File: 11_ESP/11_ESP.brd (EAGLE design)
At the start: 67.4 x 44.8 mm, 8 parts, among them T1 BC847, T2 BC847, X1 ALLSERIALSLAVE

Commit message: Use lib elements
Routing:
- removed copper zone on layer 16, net N$10
- removed copper zone on layer 16, net N$11
- removed copper zone on layer 1, net N$13
- removed copper zone on layer 16, net N$13
- removed copper zone on layer 1, net N$14
- removed copper zone on layer 16, net N$14
- removed copper zone on layer 1, net N$15
- removed copper zone on layer 16, net N$15
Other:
- board text added: "AllSerial ESP PROG v1.0 44/18"
- board text removed: "AllSerial ESP PROG v1.1 46/18"
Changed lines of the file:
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@@
 <?xml version="1.0" encoding="utf-8"?>
 <!DOCTYPE eagle SYSTEM "eagle.dtd">
-<eagle version="7.7.0">
+<eagle version="7.6.0">
 <drawing>
 <settings>
@@
 <grid distance="1.27" unitdist="mm" unit="mm" style="lines" multiple="1" display="yes" altdistance="0.025" altunitdist="inch" altunit="inch"/>
 <layers>
-<layer number="1" name="Top" color="4" fill="1" visible="yes" active="yes"/>
+<layer number="1" name="Top" color="4" fill="1" visible="no" active="yes"/>
 <layer number="2" name="Route2" color="1" fill="3" visible="no" active="no"/>
 <layer number="3" name="Route3" color="4" fill="3" visible="no" active="no"/>
@@
 <layer number="14" name="Route14" color="1" fill="6" visible="no" active="no"/>
 <layer number="15" name="Route15" color="4" fill="6" visible="no" active="no"/>
-<layer number="16" name="Bottom" color="1" fill="1" visible="yes" active="yes"/>
+<layer number="16" name="Bottom" color="1" fill="1" visible="no" active="yes"/>
 <layer number="17" name="Pads" color="2" fill="1" visible="yes" active="yes"/>
-<layer number="18" name="Vias" color="2" fill="1" visible="yes" active="yes"/>
+<layer number="18" name="Vias" color="2" fill="1" visible="no" active="yes"/>
 <layer number="19" name="Unrouted" color="6" fill="1" visible="yes" active="yes"/>
 <layer number="20" name="Dimension" color="15" fill="1" visible="yes" active="yes"/>
@@
 <layer number="24" name="bOrigins" color="15" fill="1" visible="no" active="yes"/>
 <layer number="25" name="tNames" color="7" fill="1" visible="yes" active="yes"/>
-<layer number="26" name="bNames" color="7" fill="1" visible="yes" active="yes"/>
+<layer number="26" name="bNames" color="7" fill="1" visible="no" active="yes"/>
 <layer number="27" name="tValues" color="7" fill="1" visible="yes" active="yes"/>
 <layer number="28" name="bValues" color="7" fill="1" visible="no" active="yes"/>
-<layer number="29" name="tStop" color="7" fill="3" visible="yes" active="yes"/>
-<layer number="30" name="bStop" color="7" fill="6" visible="yes" active="yes"/>
+<layer number="29" name="tStop" color="7" fill="3" visible="no" active="yes"/>
+<layer number="30" name="bStop" color="7" fill="6" visible="no" active="yes"/>
 <layer number="31" name="tCream" color="7" fill="4" visible="no" active="yes"/>
 <layer number="32" name="bCream" color="7" fill="5" visible="no" active="yes"/>
@@
 <board>
 <plain>
-<text x="-29.845" y="1.27" size="1.6764" layer="21" rot="R90">AllSerial ESP PROG v1.1 46/18</text>
-<polygon width="0.254" layer="29">
-<vertex x="-25.4" y="44.45"/>
-<vertex x="-28.575" y="44.45"/>
-<vertex x="-28.575" y="41.91"/>
-<vertex x="-25.4" y="41.91"/>
-</polygon>
-<polygon width="0.254" layer="29">
-<vertex x="-2.54" y="44.45"/>
-<vertex x="2.54" y="44.45"/>
-<vertex x="2.54" y="41.91"/>
-<vertex x="-2.54" y="41.91"/>
-</polygon>
-<polygon width="0.254" layer="29">
-<vertex x="25.4" y="44.45"/>
-<vertex x="28.575" y="44.45"/>
-<vertex x="28.575" y="41.91"/>
-<vertex x="25.4" y="41.91"/>
-</polygon>
-<polygon width="0.254" layer="30">
-<vertex x="-29.21" y="44.45"/>
-<vertex x="-25.4" y="44.45"/>
-<vertex x="-25.4" y="41.91"/>
-<vertex x="-29.21" y="41.91"/>
-</polygon>
-<polygon width="0.254" layer="30">
-<vertex x="-15.24" y="44.45"/>
-<vertex x="-11.43" y="44.45"/>
-<vertex x="-11.43" y="41.91"/>
-<vertex x="-15.24" y="41.91"/>
-</polygon>
-<polygon width="0.254" layer="30">
-<vertex x="-2.54" y="44.45"/>
-<vertex x="2.54" y="44.45"/>
-<vertex x="2.54" y="41.91"/>
-<vertex x="-2.54" y="41.91"/>
-</polygon>
-<polygon width="0.254" layer="30">
-<vertex x="11.43" y="44.45"/>
-<vertex x="15.24" y="44.45"/>
-<vertex x="15.24" y="41.91"/>
-<vertex x="11.43" y="41.91"/>
-</polygon>
-<polygon width="0.254" layer="30">
-<vertex x="25.4" y="44.45"/>
-<vertex x="29.21" y="44.45"/>
-<vertex x="29.21" y="41.91"/>
-<vertex x="25.4" y="41.91"/>
-</polygon>
+<text x="-29.845" y="1.27" size="1.6764" layer="21" rot="R90">AllSerial ESP PROG v1.0 44/18</text>
+<rectangle x1="-8.89" y1="43.815" x2="-3.81" y2="45.72" layer="29"/>
+<rectangle x1="-25.4" y1="43.815" x2="-20.32" y2="45.72" layer="29"/>
+<rectangle x1="-1.27" y1="43.815" x2="3.81" y2="45.72" layer="29"/>
+<rectangle x1="21.59" y1="43.815" x2="26.67" y2="45.72" layer="29"/>
+<rectangle x1="-2.54" y1="43.815" x2="2.54" y2="45.72" layer="30"/>
+<rectangle x1="-12.7" y1="43.815" x2="-7.62" y2="45.72" layer="30"/>
+<rectangle x1="-22.86" y1="43.815" x2="-17.78" y2="45.72" layer="30"/>
+<rectangle x1="7.62" y1="43.815" x2="12.7" y2="45.72" layer="30"/>
+<rectangle x1="17.78" y1="43.815" x2="22.86" y2="45.72" layer="30"/>
 </plain>
 <attributes>
@@
 <signal name="GND">
 <polygon width="0.254" layer="16">
-<vertex x="-34.29" y="40.64"/>
-<vertex x="34.29" y="40.64"/>
+<vertex x="-34.29" y="45.72"/>
+<vertex x="34.29" y="45.72"/>
 <vertex x="34.29" y="0"/>
 <vertex x="-34.29" y="0"/>
@@
 <vertex x="-34.29" y="0"/>
 <vertex x="34.29" y="0"/>
-<vertex x="34.29" y="40.64"/>
-<vertex x="-34.29" y="40.64"/>
+<vertex x="34.29" y="45.72"/>
+<vertex x="-34.29" y="45.72"/>
 </polygon>
 <contactref element="X1" pad="1"/>
-<via x="-7.62" y="39.37" extent="1-16" drill="0.3"/>
-<via x="-17.78" y="39.37" extent="1-16" drill="0.3"/>
-<via x="-27.94" y="39.37" extent="1-16" drill="0.3"/>
+<via x="-7.62" y="43.18" extent="1-16" drill="0.3"/>
+<via x="-17.78" y="43.18" extent="1-16" drill="0.3"/>
+<via x="-27.94" y="43.18" extent="1-16" drill="0.3"/>
 <via x="-27.94" y="35.56" extent="1-16" drill="0.3"/>
 <via x="-17.78" y="35.56" extent="1-16" drill="0.3"/>
@@
 <via x="7.62" y="30.48" extent="1-16" drill="0.3"/>
 <via x="7.62" y="35.56" extent="1-16" drill="0.3"/>
-<via x="7.62" y="39.37" extent="1-16" drill="0.3"/>
-<via x="17.78" y="39.37" extent="1-16" drill="0.3"/>
+<via x="7.62" y="43.18" extent="1-16" drill="0.3"/>
+<via x="17.78" y="43.18" extent="1-16" drill="0.3"/>
 <via x="17.78" y="35.56" extent="1-16" drill="0.3"/>
-<via x="27.94" y="39.37" extent="1-16" drill="0.3"/>
+<via x="27.94" y="43.18" extent="1-16" drill="0.3"/>
 <via x="27.94" y="35.56" extent="1-16" drill="0.3"/>
 <via x="17.78" y="25.4" extent="1-16" drill="0.3"/>
@@
 <wire x1="6.35" y1="2.54" x2="6.35" y2="4.445" width="0.3048" layer="1"/>
 </signal>
-<signal name="N$13">
-<polygon width="0.254" layer="16">
-<vertex x="-25.4" y="44.45"/>
-<vertex x="-29.21" y="44.45"/>
-<vertex x="-29.21" y="41.91"/>
-<vertex x="-25.4" y="41.91"/>
-</polygon>
-<polygon width="0.254" layer="1">
-<vertex x="-25.4" y="44.45"/>
-<vertex x="-28.575" y="44.45"/>
-<vertex x="-28.575" y="41.91"/>
-<vertex x="-25.4" y="41.91"/>
-</polygon>
-<via x="-26.035" y="43.18" extent="1-16" drill="0.3"/>
-<via x="-27.94" y="43.18" extent="1-16" drill="0.3"/>
-</signal>
-<signal name="N$14">
-<polygon width="0.254" layer="16">
-<vertex x="-2.54" y="44.45"/>
-<vertex x="2.54" y="44.45"/>
-<vertex x="2.54" y="41.91"/>
-<vertex x="-2.54" y="41.91"/>
-</polygon>
-<polygon width="0.254" layer="1">
-<vertex x="-2.54" y="44.45"/>
-<vertex x="2.54" y="44.45"/>
-<vertex x="2.54" y="41.91"/>
-<vertex x="-2.54" y="41.91"/>
-</polygon>
-<via x="0" y="43.18" extent="1-16" drill="0.3"/>
-<via x="-1.905" y="43.18" extent="1-16" drill="0.3"/>
-<via x="1.905" y="43.18" extent="1-16" drill="0.3"/>
-</signal>
-<signal name="N$15">
-<polygon width="0.254" layer="16">
-<vertex x="25.4" y="44.45"/>
-<vertex x="29.21" y="44.45"/>
-<vertex x="29.21" y="41.91"/>
-<vertex x="25.4" y="41.91"/>
-</polygon>
-<polygon width="0.254" layer="1">
-<vertex x="25.4" y="44.45"/>
-<vertex x="28.575" y="44.45"/>
-<vertex x="28.575" y="41.91"/>
-<vertex x="25.4" y="41.91"/>
-</polygon>
-<via x="26.035" y="43.18" extent="1-16" drill="0.3"/>
-<via x="27.94" y="43.18" extent="1-16" drill="0.3"/>
-</signal>
-<signal name="N$10">
-<polygon width="0.254" layer="16">
-<vertex x="-15.24" y="44.45"/>
-<vertex x="-11.43" y="44.45"/>
-<vertex x="-11.43" y="41.91"/>
-<vertex x="-15.24" y="41.91"/>
-</polygon>
-<via x="-13.335" y="43.18" extent="1-16" drill="0.3"/>
-<via x="-14.605" y="43.18" extent="1-16" drill="0.3"/>
-<via x="-12.065" y="43.18" extent="1-16" drill="0.3"/>
-</signal>
-<signal name="N$11">
-<polygon width="0.254" layer="16">
-<vertex x="11.43" y="44.45"/>
-<vertex x="15.24" y="44.45"/>
-<vertex x="15.24" y="41.91"/>
-<vertex x="11.43" y="41.91"/>
-</polygon>
-<via x="13.335" y="43.18" extent="1-16" drill="0.3"/>
-<via x="12.065" y="43.18" extent="1-16" drill="0.3"/>
-<via x="14.605" y="43.18" extent="1-16" drill="0.3"/>
-</signal>
 </signals>

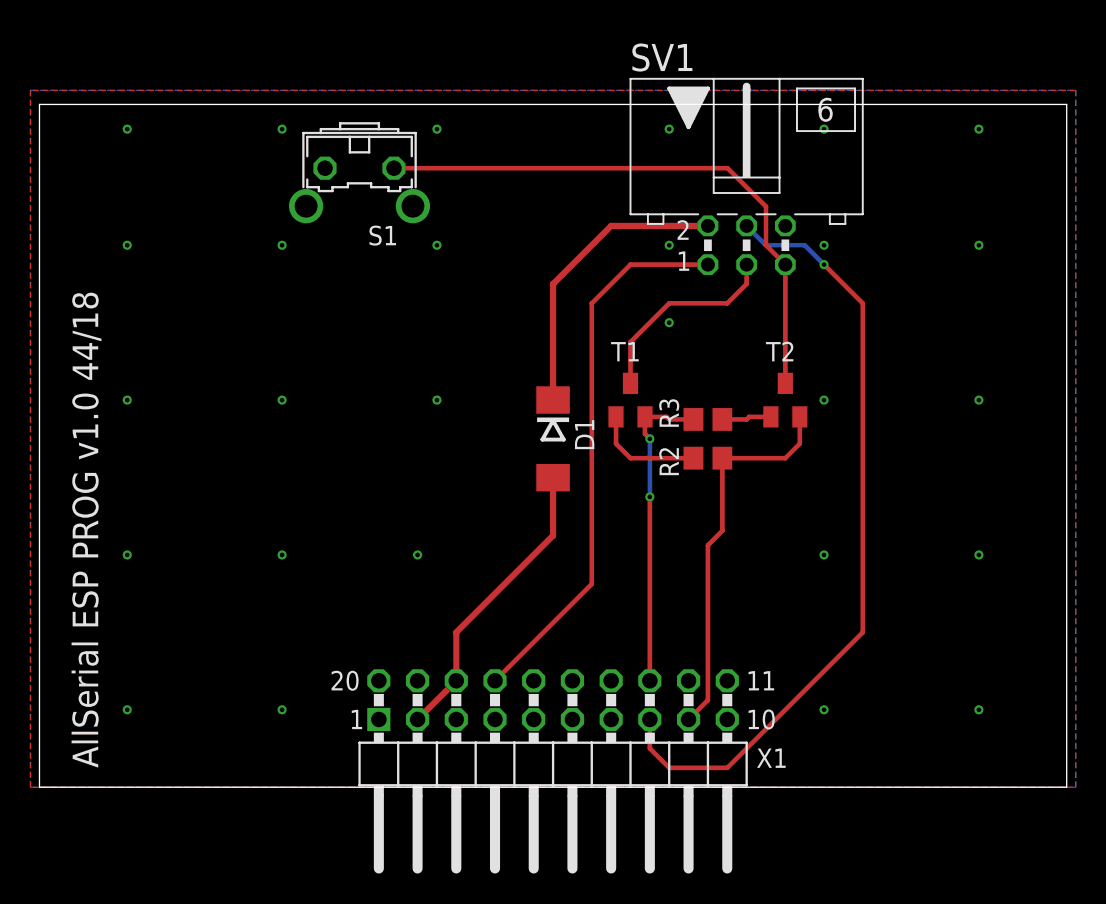
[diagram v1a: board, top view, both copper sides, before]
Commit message: pro mini layout corrected
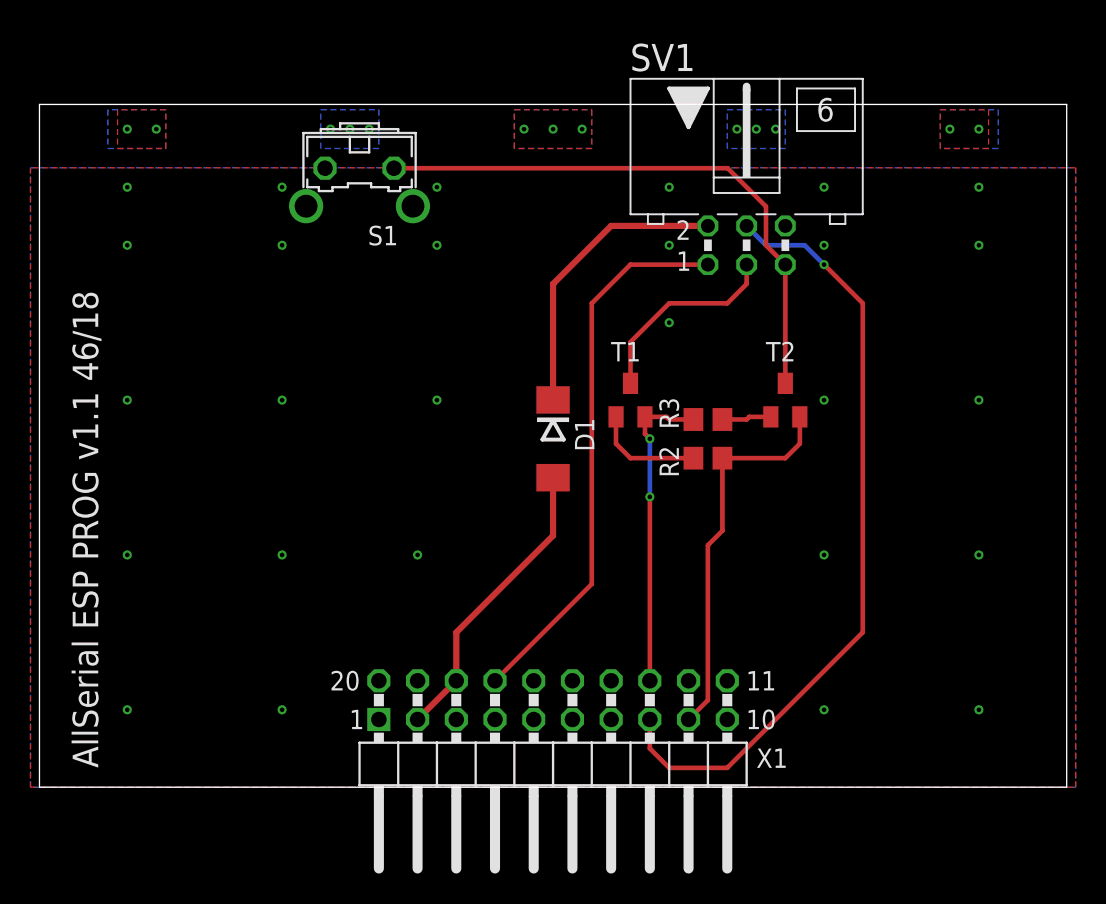
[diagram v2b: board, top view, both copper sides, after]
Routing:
- added copper zone on layer 16, net N$10
- added copper zone on layer 16, net N$11
- added copper zone on layer 1, net N$13
- added copper zone on layer 16, net N$13
- added copper zone on layer 1, net N$14
- added copper zone on layer 16, net N$14
- added copper zone on layer 1, net N$15
- added copper zone on layer 16, net N$15
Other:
- board text added: "AllSerial ESP PROG v1.1 46/18"
- board text removed: "AllSerial ESP PROG v1.0 44/18"
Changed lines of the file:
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@@
 <?xml version="1.0" encoding="utf-8"?>
 <!DOCTYPE eagle SYSTEM "eagle.dtd">
-<eagle version="7.6.0">
+<eagle version="7.7.0">
 <drawing>
 <settings>
@@
 <grid distance="1.27" unitdist="mm" unit="mm" style="lines" multiple="1" display="yes" altdistance="0.025" altunitdist="inch" altunit="inch"/>
 <layers>
-<layer number="1" name="Top" color="4" fill="1" visible="no" active="yes"/>
+<layer number="1" name="Top" color="4" fill="1" visible="yes" active="yes"/>
 <layer number="2" name="Route2" color="1" fill="3" visible="no" active="no"/>
 <layer number="3" name="Route3" color="4" fill="3" visible="no" active="no"/>
@@
 <layer number="14" name="Route14" color="1" fill="6" visible="no" active="no"/>
 <layer number="15" name="Route15" color="4" fill="6" visible="no" active="no"/>
-<layer number="16" name="Bottom" color="1" fill="1" visible="no" active="yes"/>
+<layer number="16" name="Bottom" color="1" fill="1" visible="yes" active="yes"/>
 <layer number="17" name="Pads" color="2" fill="1" visible="yes" active="yes"/>
-<layer number="18" name="Vias" color="2" fill="1" visible="no" active="yes"/>
+<layer number="18" name="Vias" color="2" fill="1" visible="yes" active="yes"/>
 <layer number="19" name="Unrouted" color="6" fill="1" visible="yes" active="yes"/>
 <layer number="20" name="Dimension" color="15" fill="1" visible="yes" active="yes"/>
@@
 <layer number="24" name="bOrigins" color="15" fill="1" visible="no" active="yes"/>
 <layer number="25" name="tNames" color="7" fill="1" visible="yes" active="yes"/>
-<layer number="26" name="bNames" color="7" fill="1" visible="no" active="yes"/>
+<layer number="26" name="bNames" color="7" fill="1" visible="yes" active="yes"/>
 <layer number="27" name="tValues" color="7" fill="1" visible="yes" active="yes"/>
 <layer number="28" name="bValues" color="7" fill="1" visible="no" active="yes"/>
-<layer number="29" name="tStop" color="7" fill="3" visible="no" active="yes"/>
-<layer number="30" name="bStop" color="7" fill="6" visible="no" active="yes"/>
+<layer number="29" name="tStop" color="7" fill="3" visible="yes" active="yes"/>
+<layer number="30" name="bStop" color="7" fill="6" visible="yes" active="yes"/>
 <layer number="31" name="tCream" color="7" fill="4" visible="no" active="yes"/>
 <layer number="32" name="bCream" color="7" fill="5" visible="no" active="yes"/>
@@
 <board>
 <plain>
-<text x="-29.845" y="1.27" size="1.6764" layer="21" rot="R90">AllSerial ESP PROG v1.0 44/18</text>
-<rectangle x1="-8.89" y1="43.815" x2="-3.81" y2="45.72" layer="29"/>
-<rectangle x1="-25.4" y1="43.815" x2="-20.32" y2="45.72" layer="29"/>
-<rectangle x1="-1.27" y1="43.815" x2="3.81" y2="45.72" layer="29"/>
-<rectangle x1="21.59" y1="43.815" x2="26.67" y2="45.72" layer="29"/>
-<rectangle x1="-2.54" y1="43.815" x2="2.54" y2="45.72" layer="30"/>
-<rectangle x1="-12.7" y1="43.815" x2="-7.62" y2="45.72" layer="30"/>
-<rectangle x1="-22.86" y1="43.815" x2="-17.78" y2="45.72" layer="30"/>
-<rectangle x1="7.62" y1="43.815" x2="12.7" y2="45.72" layer="30"/>
-<rectangle x1="17.78" y1="43.815" x2="22.86" y2="45.72" layer="30"/>
+<text x="-29.845" y="1.27" size="1.6764" layer="21" rot="R90">AllSerial ESP PROG v1.1 46/18</text>
+<polygon width="0.254" layer="29">
+<vertex x="-25.4" y="44.45"/>
+<vertex x="-28.575" y="44.45"/>
+<vertex x="-28.575" y="41.91"/>
+<vertex x="-25.4" y="41.91"/>
+</polygon>
+<polygon width="0.254" layer="29">
+<vertex x="-2.54" y="44.45"/>
+<vertex x="2.54" y="44.45"/>
+<vertex x="2.54" y="41.91"/>
+<vertex x="-2.54" y="41.91"/>
+</polygon>
+<polygon width="0.254" layer="29">
+<vertex x="25.4" y="44.45"/>
+<vertex x="28.575" y="44.45"/>
+<vertex x="28.575" y="41.91"/>
+<vertex x="25.4" y="41.91"/>
+</polygon>
+<polygon width="0.254" layer="30">
+<vertex x="-29.21" y="44.45"/>
+<vertex x="-25.4" y="44.45"/>
+<vertex x="-25.4" y="41.91"/>
+<vertex x="-29.21" y="41.91"/>
+</polygon>
+<polygon width="0.254" layer="30">
+<vertex x="-15.24" y="44.45"/>
+<vertex x="-11.43" y="44.45"/>
+<vertex x="-11.43" y="41.91"/>
+<vertex x="-15.24" y="41.91"/>
+</polygon>
+<polygon width="0.254" layer="30">
+<vertex x="-2.54" y="44.45"/>
+<vertex x="2.54" y="44.45"/>
+<vertex x="2.54" y="41.91"/>
+<vertex x="-2.54" y="41.91"/>
+</polygon>
+<polygon width="0.254" layer="30">
+<vertex x="11.43" y="44.45"/>
+<vertex x="15.24" y="44.45"/>
+<vertex x="15.24" y="41.91"/>
+<vertex x="11.43" y="41.91"/>
+</polygon>
+<polygon width="0.254" layer="30">
+<vertex x="25.4" y="44.45"/>
+<vertex x="29.21" y="44.45"/>
+<vertex x="29.21" y="41.91"/>
+<vertex x="25.4" y="41.91"/>
+</polygon>
 </plain>
 <attributes>
@@
 <signal name="GND">
 <polygon width="0.254" layer="16">
-<vertex x="-34.29" y="45.72"/>
-<vertex x="34.29" y="45.72"/>
+<vertex x="-34.29" y="40.64"/>
+<vertex x="34.29" y="40.64"/>
 <vertex x="34.29" y="0"/>
 <vertex x="-34.29" y="0"/>
@@
 <vertex x="-34.29" y="0"/>
 <vertex x="34.29" y="0"/>
-<vertex x="34.29" y="45.72"/>
-<vertex x="-34.29" y="45.72"/>
+<vertex x="34.29" y="40.64"/>
+<vertex x="-34.29" y="40.64"/>
 </polygon>
 <contactref element="X1" pad="1"/>
-<via x="-7.62" y="43.18" extent="1-16" drill="0.3"/>
-<via x="-17.78" y="43.18" extent="1-16" drill="0.3"/>
-<via x="-27.94" y="43.18" extent="1-16" drill="0.3"/>
+<via x="-7.62" y="39.37" extent="1-16" drill="0.3"/>
+<via x="-17.78" y="39.37" extent="1-16" drill="0.3"/>
+<via x="-27.94" y="39.37" extent="1-16" drill="0.3"/>
 <via x="-27.94" y="35.56" extent="1-16" drill="0.3"/>
 <via x="-17.78" y="35.56" extent="1-16" drill="0.3"/>
@@
 <via x="7.62" y="30.48" extent="1-16" drill="0.3"/>
 <via x="7.62" y="35.56" extent="1-16" drill="0.3"/>
-<via x="7.62" y="43.18" extent="1-16" drill="0.3"/>
-<via x="17.78" y="43.18" extent="1-16" drill="0.3"/>
+<via x="7.62" y="39.37" extent="1-16" drill="0.3"/>
+<via x="17.78" y="39.37" extent="1-16" drill="0.3"/>
 <via x="17.78" y="35.56" extent="1-16" drill="0.3"/>
-<via x="27.94" y="43.18" extent="1-16" drill="0.3"/>
+<via x="27.94" y="39.37" extent="1-16" drill="0.3"/>
 <via x="27.94" y="35.56" extent="1-16" drill="0.3"/>
 <via x="17.78" y="25.4" extent="1-16" drill="0.3"/>
@@
 <wire x1="6.35" y1="2.54" x2="6.35" y2="4.445" width="0.3048" layer="1"/>
 </signal>
+<signal name="N$13">
+<polygon width="0.254" layer="16">
+<vertex x="-25.4" y="44.45"/>
+<vertex x="-29.21" y="44.45"/>
+<vertex x="-29.21" y="41.91"/>
+<vertex x="-25.4" y="41.91"/>
+</polygon>
+<polygon width="0.254" layer="1">
+<vertex x="-25.4" y="44.45"/>
+<vertex x="-28.575" y="44.45"/>
+<vertex x="-28.575" y="41.91"/>
+<vertex x="-25.4" y="41.91"/>
+</polygon>
+<via x="-26.035" y="43.18" extent="1-16" drill="0.3"/>
+<via x="-27.94" y="43.18" extent="1-16" drill="0.3"/>
+</signal>
+<signal name="N$14">
+<polygon width="0.254" layer="16">
+<vertex x="-2.54" y="44.45"/>
+<vertex x="2.54" y="44.45"/>
+<vertex x="2.54" y="41.91"/>
+<vertex x="-2.54" y="41.91"/>
+</polygon>
+<polygon width="0.254" layer="1">
+<vertex x="-2.54" y="44.45"/>
+<vertex x="2.54" y="44.45"/>
+<vertex x="2.54" y="41.91"/>
+<vertex x="-2.54" y="41.91"/>
+</polygon>
+<via x="0" y="43.18" extent="1-16" drill="0.3"/>
+<via x="-1.905" y="43.18" extent="1-16" drill="0.3"/>
+<via x="1.905" y="43.18" extent="1-16" drill="0.3"/>
+</signal>
+<signal name="N$15">
+<polygon width="0.254" layer="16">
+<vertex x="25.4" y="44.45"/>
+<vertex x="29.21" y="44.45"/>
+<vertex x="29.21" y="41.91"/>
+<vertex x="25.4" y="41.91"/>
+</polygon>
+<polygon width="0.254" layer="1">
+<vertex x="25.4" y="44.45"/>
+<vertex x="28.575" y="44.45"/>
+<vertex x="28.575" y="41.91"/>
+<vertex x="25.4" y="41.91"/>
+</polygon>
+<via x="26.035" y="43.18" extent="1-16" drill="0.3"/>
+<via x="27.94" y="43.18" extent="1-16" drill="0.3"/>
+</signal>
+<signal name="N$10">
+<polygon width="0.254" layer="16">
+<vertex x="-15.24" y="44.45"/>
+<vertex x="-11.43" y="44.45"/>
+<vertex x="-11.43" y="41.91"/>
+<vertex x="-15.24" y="41.91"/>
+</polygon>
+<via x="-13.335" y="43.18" extent="1-16" drill="0.3"/>
+<via x="-14.605" y="43.18" extent="1-16" drill="0.3"/>
+<via x="-12.065" y="43.18" extent="1-16" drill="0.3"/>
+</signal>
+<signal name="N$11">
+<polygon width="0.254" layer="16">
+<vertex x="11.43" y="44.45"/>
+<vertex x="15.24" y="44.45"/>
+<vertex x="15.24" y="41.91"/>
+<vertex x="11.43" y="41.91"/>
+</polygon>
+<via x="13.335" y="43.18" extent="1-16" drill="0.3"/>
+<via x="12.065" y="43.18" extent="1-16" drill="0.3"/>
+<via x="14.605" y="43.18" extent="1-16" drill="0.3"/>
+</signal>
 </signals>
